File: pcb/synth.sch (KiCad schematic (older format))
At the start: 65 parts, among them J1 Conn_01x06, J2 Barrel_Jack_Switch, SW1 SW_Push, SW10 SW_Push, SW11 SW_Push, SW12 SW_Push, SW13 SW_Push, SW14 SW_Push, SW15 SW_Push, SW16 SW_Push, SW17 SW_Push, SW18 SW_Push, SW19 SW_Push, SW2 SW_Push, SW20 SW_Push, SW21 SW_Push, SW22 SW_Push, SW23 SW_Push, SW24 SW_Push, SW25 SW_Push, SW26 SW_Push, SW27 SW_Push, SW28 SW_Push, SW29 SW_Push, SW3 SW_Push, SW30 SW_Push, SW4 SW_Push, SW5 SW_Push, SW6 SW_Push, SW7 SW_Push, SW8 SW_Push, SW9 SW_Push, U1 LD1117S33TR_SOT223, U2 STM32F407VGTx, Y1 Crystal_8

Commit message: A bunch of routing and footprint changes.
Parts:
- C1, C10, C11, C12, C14, C15, C16, C18, C19, C2, C3, C4, C5, C6, C8: footprint Capacitor_THT:CP_Axial_L11.0mm_D8.0mm_P15.00mm_Horizontal -> Capacitor_THT:C_Disc_D3.0mm_W2.0mm_P2.50mm
- C13, C7: footprint (none) -> Capacitor_THT:C_Disc_D3.0mm_W2.0mm_P2.50mm
- R2, R3: footprint Resistor_THT:R_Axial_DIN0207_L6.3mm_D2.5mm_P2.54mm_Vertical -> Resistor_THT:R_Axial_DIN0204_L3.6mm_D1.6mm_P5.08mm_Horizontal
- RV1, RV2, RV3, RV4, RV5, RV6, RV7, RV8: footprint Potentiometer_THT:Potentiometer_Bourns_3005_Horizontal -> Potentiometer_THT:Potentiometer_Bourns_PTV09A-1_Single_Vertical
- Y1: footprint Crystal:Crystal_AT310_D3.0mm_L10.0mm_Horizontal -> Synth_Footprints:ATS08A
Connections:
- wire segments 209 -> 233

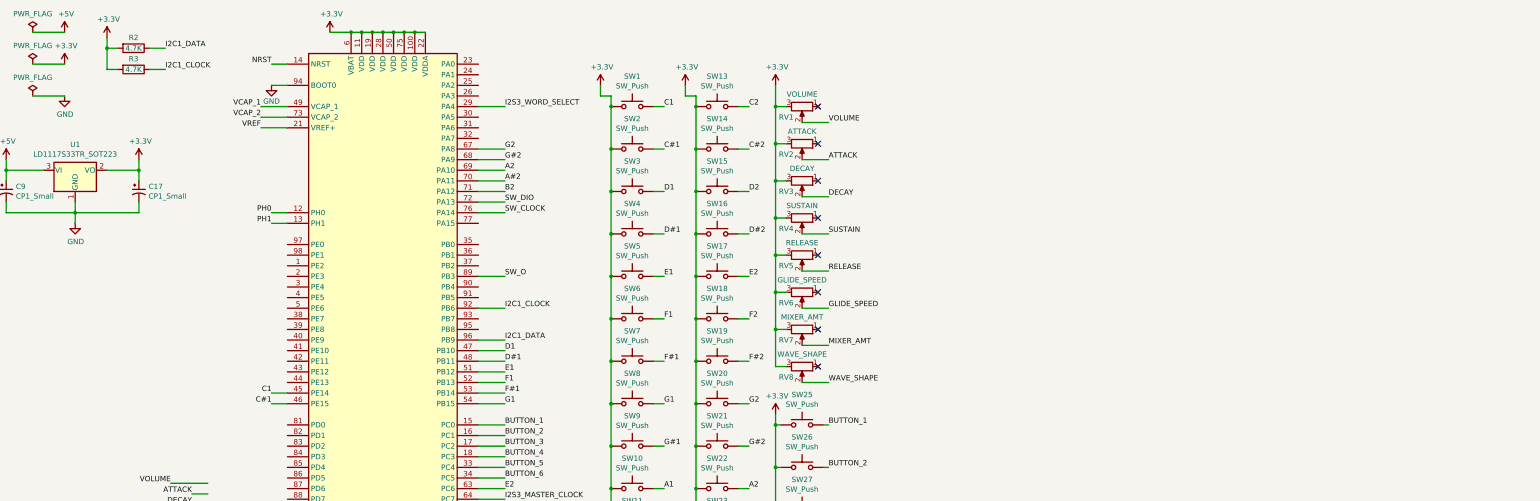
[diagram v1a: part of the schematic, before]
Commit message: A ton of changes.
- Redid the routing for the keyboard.
- Added LEDs for Arp style and scale with accompanying driver.
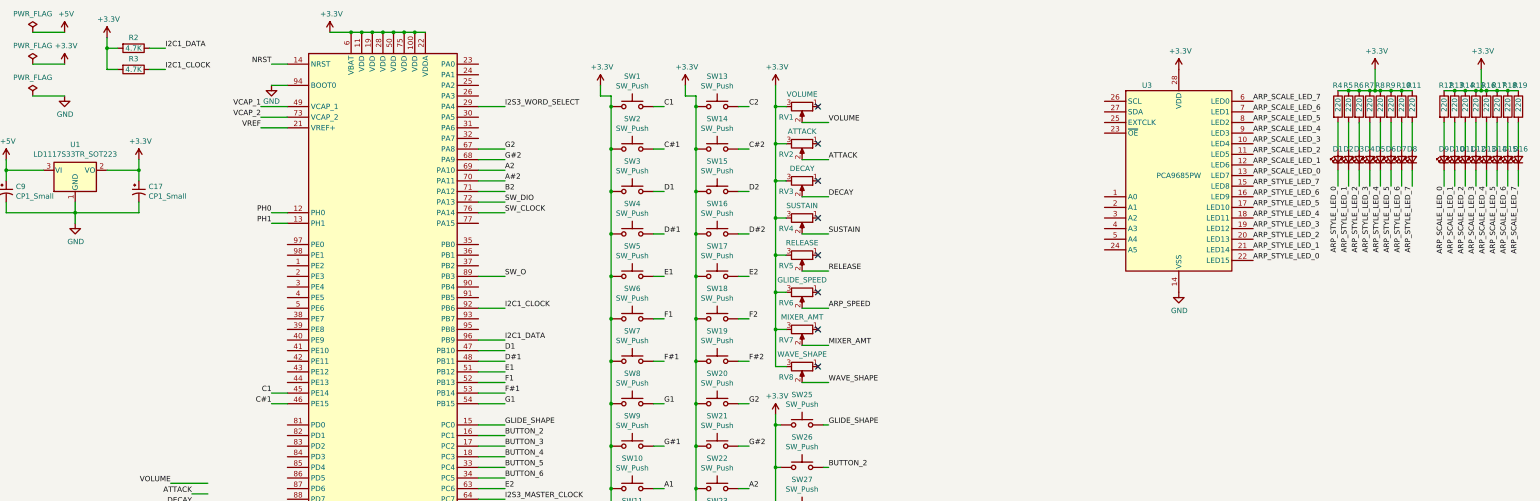
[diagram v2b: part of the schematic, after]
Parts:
- added D1, D10, D11, D12, D13, D14, D15, D16, D2, D3, D4, D5, D6, D7, D8, D9: LED_Small, LED_SMD:LED_0805_2012Metric, symbol Device:LED_Small
- added R10, R11, R12, R13, R14, R15, R16, R17, R18, R19, R4, R5, R6, R7, R8, R9: 220, Resistor_SMD:R_0805_2012Metric, symbol Device:R
- added U3: PCA9685PW, Package_SO:TSSOP-28_4.4x9.7mm_P0.65mm, symbol Driver_LED:PCA9685PW
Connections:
- net labels added: ARP_SCALE_LED_0, ARP_SCALE_LED_1, ARP_SCALE_LED_2, ARP_SCALE_LED_3, ARP_SCALE_LED_4, ARP_SCALE_LED_5, ARP_SCALE_LED_6, ARP_SCALE_LED_7, ARP_SPEED, ARP_STYLE_LED_0, ARP_STYLE_LED_1, ARP_STYLE_LED_2, ARP_STYLE_LED_3, ARP_STYLE_LED_4, ARP_STYLE_LED_5, ARP_STYLE_LED_6, ARP_STYLE_LED_7, GLIDE_SHAPE
- net labels removed: BUTTON_1
- wire segments 233 -> 283

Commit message: Add CS43L22 audio DAC.
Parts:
- added J3: AudioJack3, Connector_Audio:Jack_3.5mm_CUI_SJ1-3533NG_Horizontal, symbol Connector:AudioJack3
- added U4: CS43L22, Package_DFN_QFN:QFN-40-1EP_6x6mm_P0.5mm_EP4.6x4.6mm, symbol Synth_Library:CS43L22
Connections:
- net GND: now also U4.41 (GND_PAD)
- no-connect marks 9 -> 17
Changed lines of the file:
@@
 Text Label 13650 1450 0    50   ~ 0
 ARP_SCALE_LED_7
+$Comp
+L Synth_Library:CS43L22 U4
+U 1 1 5D1FF9CB
+P 14550 5350
+F 0 "U4" H 14550 6565 50  0000 C CNN
+F 1 "CS43L22" H 14550 6474 50  0000 C CNN
+F 2 "Package_DFN_QFN:QFN-40-1EP_6x6mm_P0.5mm_EP4.6x4.6mm" H 14600 5350 50  0001 C CNN
+F 3 "" H 14600 5350 50  0001 C CNN
+	1    14550 5350
+	1    0    0    -1
+$EndComp
+NoConn ~ 15300 5400
+NoConn ~ 15300 5500
+NoConn ~ 15300 5800
+NoConn ~ 15300 5900
+NoConn ~ 15300 6000
+NoConn ~ 15300 6100
+NoConn ~ 15300 6200
+NoConn ~ 15300 6300
+$Comp
+L power:GND #PWR0105
+U 1 1 5D2D7AFA
+P 14550 6450
+F 0 "#PWR0105" H 14550 6200 50  0001 C CNN
+F 1 "GND" H 14555 6277 50  0000 C CNN
+F 2 "" H 14550 6450 50  0001 C CNN
+F 3 "" H 14550 6450 50  0001 C CNN
+	1    14550 6450
+	1    0    0    -1
+$EndComp
+$Comp
+L Connector:AudioJack3 J3
+U 1 1 5D2F03E6
+P 900 3150
+F 0 "J3" H 880 3475 50  0000 C CNN
+F 1 "AudioJack3" H 880 3384 50  0000 C CNN
+F 2 "Connector_Audio:Jack_3.5mm_CUI_SJ1-3533NG_Horizontal" H 900 3150 50  0001 C CNN
+F 3 "~" H 900 3150 50  0001 C CNN
+	1    900  3150
+	1    0    0    -1
+$EndComp
 $EndSCHEMATC

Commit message: Add about half of the schematic for the CS43L22 DAC.
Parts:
- added C? (x2): 0.022uF, symbol Device:C_Small
- added C? (x3): 0.1uF, symbol Device:C_Small
- added C?: 10uF, symbol Device:C_Small
- added C? (x2): 1uF (X7R), symbol Device:C_Small
- added C?: 1uF, symbol Device:CP1_Small
- added C? (x3): .1uF, symbol Device:C_Small
- added R? (x2): 51, symbol Device:R_Small
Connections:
- net +3V3: now also U4.33 (VL), U4.5 (VP), U4.8 (VP), C?.1, C?.1, C?.1, C?.1
- net GND: now also U4.3 (AD0), C?.2, C?.2, C?.2, C?.2, C?.2
- net I2C1_CLOCK: now also U4.2 (SCL)
- net I2C1_DATA: now also U4.1 (SDA)
- net at U4.10 (-VHPFILT): now also C?.1
- net at U4.11 (FLYN): now also C?.1
- net at U4.12 (FLYP): now also C?.2
- net +VHP: now reaches U4.13 (+VHP)
- net +VHP: now also C?.2
- net HP_RIGHT: now reaches U4.14 (HP/LINE_OUTB)
- net HP_RIGHT: now also J3.R, C?.1
- net HP_LEFT: now reaches U4.15 (HP/LINE_OUTA)
- net HP_LEFT: now also J3.T, C?.1
- net VA: now reaches U4.16 (VA)
- net VA: now also C?.2
- net VD: now reaches U4.34 (VD)
- net VD: now also C?.2
- net GNDA: now reaches J3.S
- net GNDA: now also R?.2, R?.2
- new net: C?.2, R?.1 (x2)
- new net: C?.1, C?.1, C?.1, C?.2
- new net +2V5: C?.1
- no-connect marks 17 -> 21
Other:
- moved on the sheet: C18, C19, J3, RV1, RV2, RV3, RV4, RV5, RV6, RV7, RV8, SW1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
